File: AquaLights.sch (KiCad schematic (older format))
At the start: 15 parts, among them J2 Raspberry_Pi_2_3, U1 LM2575-5.0BT

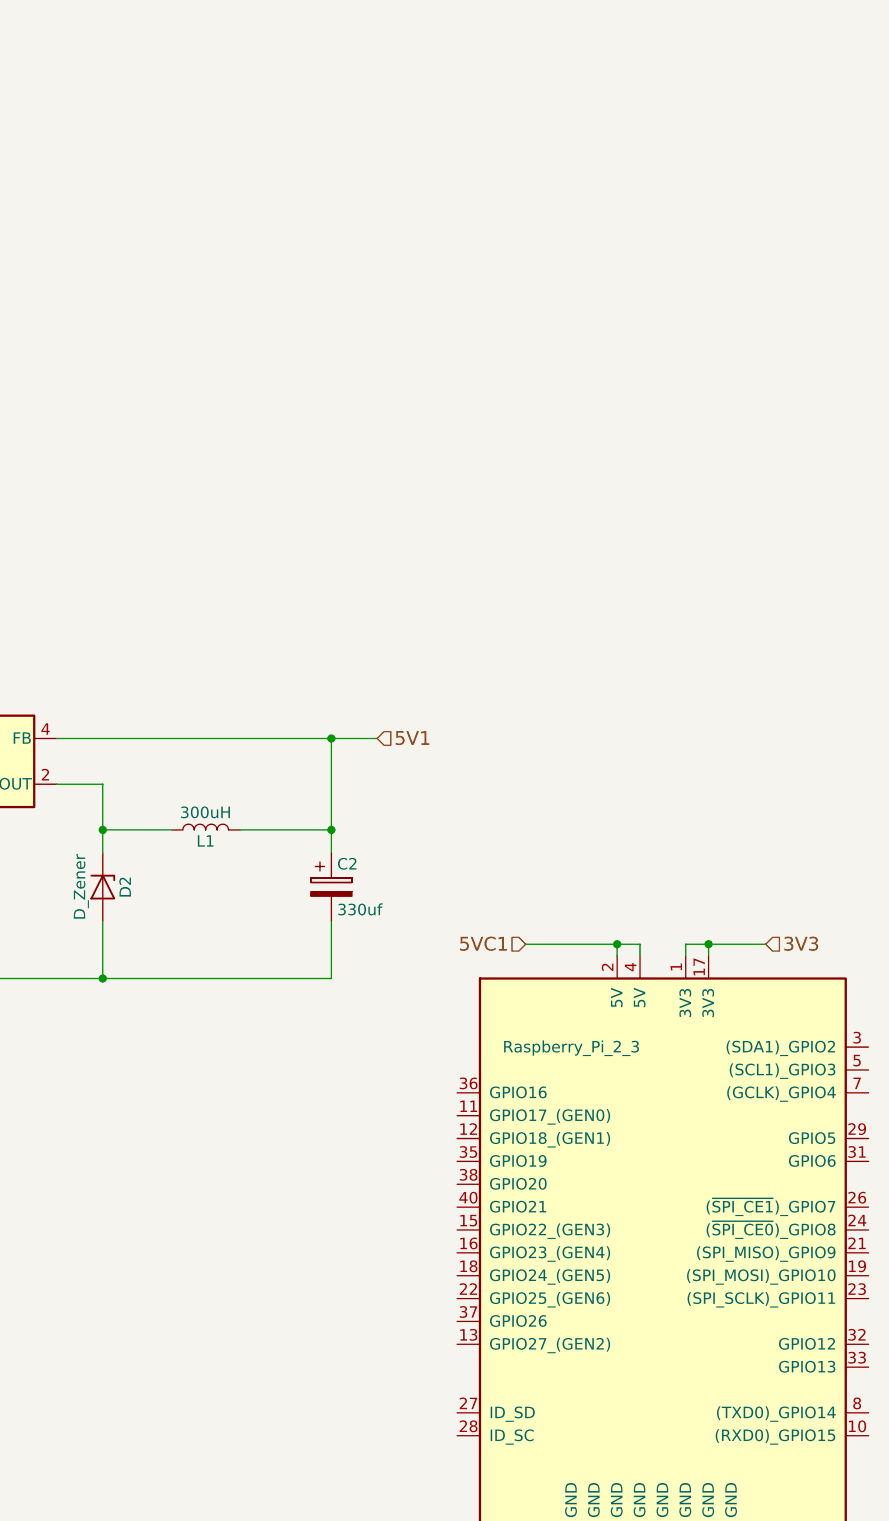
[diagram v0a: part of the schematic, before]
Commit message: Add one PWM Section
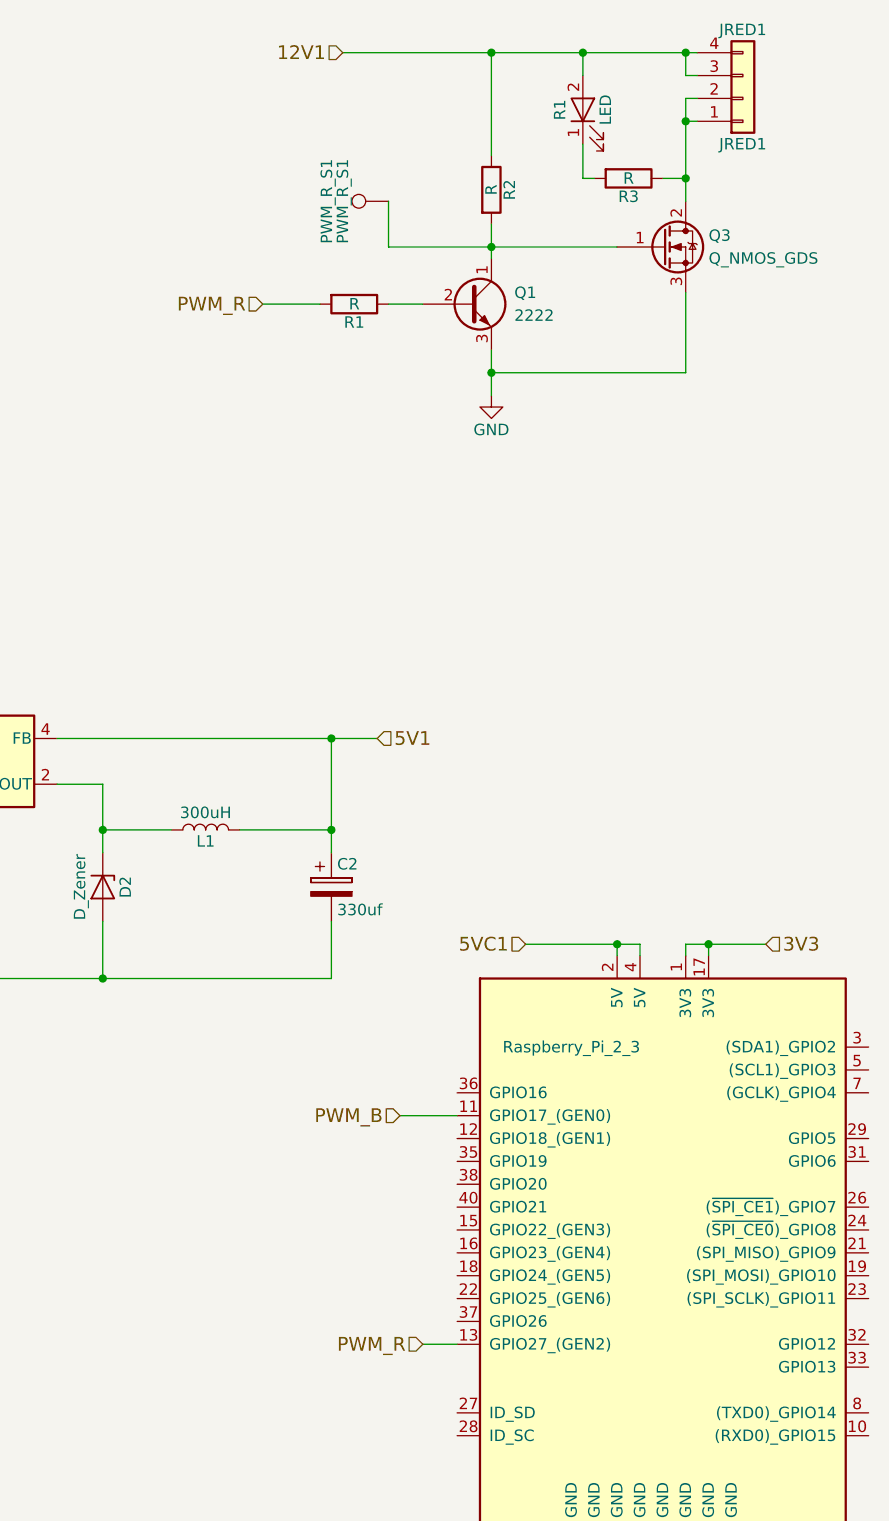
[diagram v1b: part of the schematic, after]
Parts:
- added JRED1: JRED1, symbol Conn_01x04
- added PWM_R_S1: PWM_R_S1, symbol TEST_1P
- added Q1: 2222, symbol Q_NPN_CBE
- added Q3: Q_NMOS_GDS, symbol Q_NMOS_GDS
- added R1, R2, R3: R, symbol R
- added R1: LED, symbol LED
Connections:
- net 12V1: now also JRED1.3 (Pin_3), JRED1.4 (Pin_4), R1.2 (A), R2.1
- net GND: now also Q1.3 (E), Q3.3 (S)
- net PWM_B: now reaches J2.11 (GPIO17_(GEN0))
- net PWM_R: now reaches J2.13 (GPIO27_(GEN2))
- net PWM_R: now also R1.2
- new net: Q1.2 (B), R1.1
- new net: PWM_R_S1.1, Q1.1 (C), Q3.1 (G), R2.2
- new net: JRED1.1 (Pin_1), JRED1.2 (Pin_2), Q3.2 (D), R3.1
- new net: R1.1 (K), R3.2
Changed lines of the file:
@@
 5VC1
 Connection ~ 2200 5600
+Text HLabel 4700 6400 0    60   Input ~ 0
+PWM_R
+Wire Wire Line
+	4700 6400 4850 6400
+Text HLabel 4600 5400 0    60   Input ~ 0
+PWM_B
+Wire Wire Line
+	4600 5400 4850 5400
+Text HLabel 4000 1850 0    60   Input ~ 0
+PWM_R
+$Comp
+L R R1
+U 1 1 5A3322D0
+P 4400 1850
+F 0 "R1" V 4480 1850 50  0000 C CNN
+F 1 "R" V 4400 1850 50  0000 C CNN
+F 2 "" V 4330 1850 50  0001 C CNN
+F 3 "" H 4400 1850 50  0001 C CNN
+	1    4400 1850
+	0    1    1    0
+$EndComp
+Wire Wire Line
+	4000 1850 4250 1850
+$Comp
+L Q_NPN_CBE Q1
+U 1 1 5A3324B5
+P 4900 1850
+F 0 "Q1" H 5100 1900 50  0000 L CNN
+F 1 "2222" H 5100 1800 50  0000 L CNN
+F 2 "" H 5100 1950 50  0001 C CNN
+F 3 "" H 4900 1850 50  0001 C CNN
+	1    4900 1850
+	1    0    0    -1
+$EndComp
+Wire Wire Line
+	4550 1850 4700 1850
+$Comp
+L GND #PWR?
+U 1 1 5A3325C1
+P 5000 2250
+F 0 "#PWR?" H 5000 2000 50  0001 C CNN
+F 1 "GND" H 5000 2100 50  0000 C CNN
+F 2 "" H 5000 2250 50  0001 C CNN
+F 3 "" H 5000 2250 50  0001 C CNN
+	1    5000 2250
+	1    0    0    -1
+$EndComp
+Wire Wire Line
+	5000 2050 5000 2250
+$Comp
+L R R2
+U 1 1 5A33264F
+P 5000 1350
+F 0 "R2" V 5080 1350 50  0000 C CNN
+F 1 "R" V 5000 1350 50  0000 C CNN
+F 2 "" V 4930 1350 50  0001 C CNN
+F 3 "" H 5000 1350 50  0001 C CNN
+	1    5000 1350
+	1    0    0    -1
+$EndComp
+Wire Wire Line
+	5000 1500 5000 1650
+Text HLabel 4350 750  0    60   Input ~ 0
+12V1
+Wire Wire Line
+	5000 750  5000 1200
+$Comp
+L Q_NMOS_GDS Q3
+U 1 1 5A3333B3
+P 5750 1600
+F 0 "Q3" H 5950 1650 50  0000 L CNN
+F 1 "Q_NMOS_GDS" H 5950 1550 50  0000 L CNN
+F 2 "" H 5950 1700 50  0001 C CNN
+F 3 "" H 5750 1600 50  0001 C CNN
+	1    5750 1600
+	1    0    0    -1
+$EndComp
+Wire Wire Line
+	4550 1600 5550 1600
+Connection ~ 5000 1600
+Wire Wire Line
+	5850 1800 5850 2150
+Wire Wire Line
+	5850 2150 5000 2150
+Connection ~ 5000 2150
+$Comp
+L Conn_01x04 JRED1
+U 1 1 5A3334C6
+P 6100 950
+F 0 "JRED1" H 6100 1150 50  0000 C CNN
+F 1 "JRED1" H 6100 650 50  0000 C CNN
+F 2 "" H 6100 950 50  0001 C CNN
+F 3 "" H 6100 950 50  0001 C CNN
+	1    6100 950
+	1    0    0    1
+$EndComp
+Wire Wire Line
+	5850 1400 5850 950
+Wire Wire Line
+	5850 950  5900 950
+Wire Wire Line
+	5900 1050 5850 1050
+Connection ~ 5850 1050
+Wire Wire Line
+	5900 850  5850 850
+Wire Wire Line
+	5850 850  5850 750
+Wire Wire Line
+	4350 750  5900 750
+Connection ~ 5850 750
+Connection ~ 5000 750
+$Comp
+L LED R1
+U 1 1 5A334293
+P 5400 1000
+F 0 "R1" H 5400 1100 50  0000 C CNN
+F 1 "LED" H 5400 900 50  0000 C CNN
+F 2 "" H 5400 1000 50  0001 C CNN
+F 3 "" H 5400 1000 50  0001 C CNN
+	1    5400 1000
+	0    -1   -1   0
+$EndComp
+$Comp
+L R R3
+U 1 1 5A3342DA
+P 5600 1300
+F 0 "R3" V 5680 1300 50  0000 C CNN
+F 1 "R" V 5600 1300 50  0000 C CNN
+F 2 "" V 5530 1300 50  0001 C CNN
+F 3 "" H 5600 1300 50  0001 C CNN
+	1    5600 1300
+	0    1    1    0
+$EndComp
+Wire Wire Line
+	5400 750  5400 850
+Connection ~ 5400 750
+Wire Wire Line
+	5400 1150 5400 1300
+Wire Wire Line
+	5400 1300 5450 1300
+Wire Wire Line
+	5750 1300 5850 1300
+Connection ~ 5850 1300
+$Comp
+L TEST_1P PWM_R_S1
+U 1 1 5A33462D
+P 4550 1400
+F 0 "PWM_R_S1" H 4550 1670 50  0000 C CNN
+F 1 "PWM_R_S1" H 4550 1600 50  0000 C CNN
+F 2 "" H 4750 1400 50  0001 C CNN
+F 3 "" H 4750 1400 50  0001 C CNN
+	1    4550 1400
+	0    -1   -1   0
+$EndComp
+Wire Wire Line
+	4550 1400 4550 1600
 $EndSCHEMATC

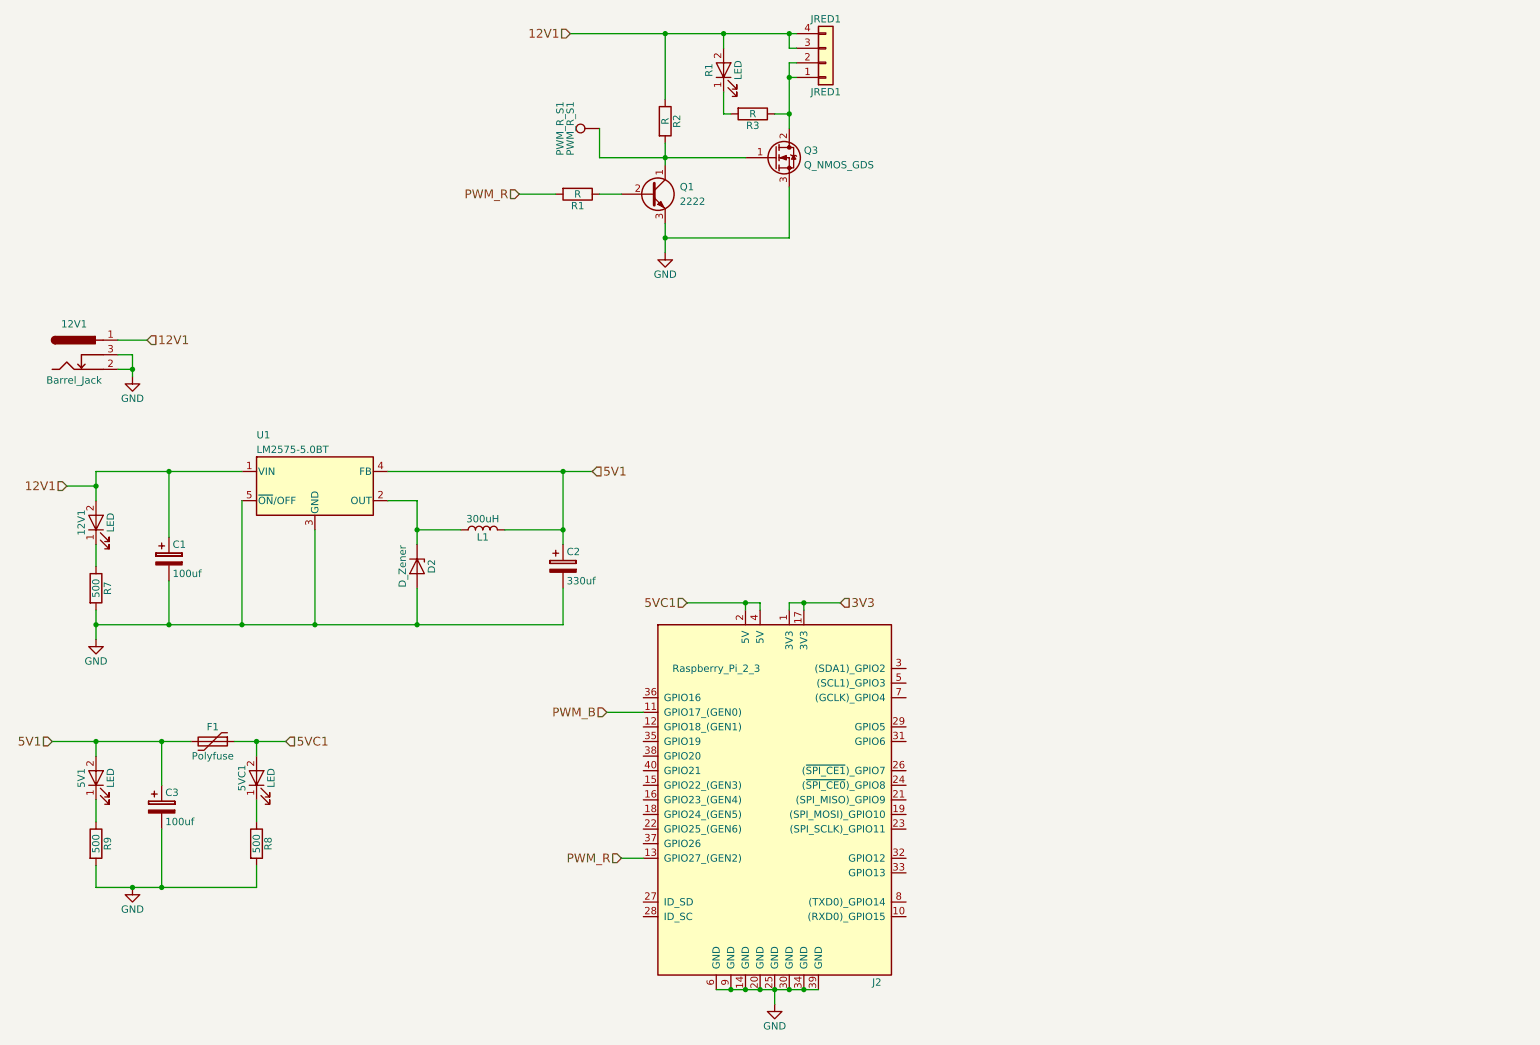
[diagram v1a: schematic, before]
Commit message: Finish PWM Sections
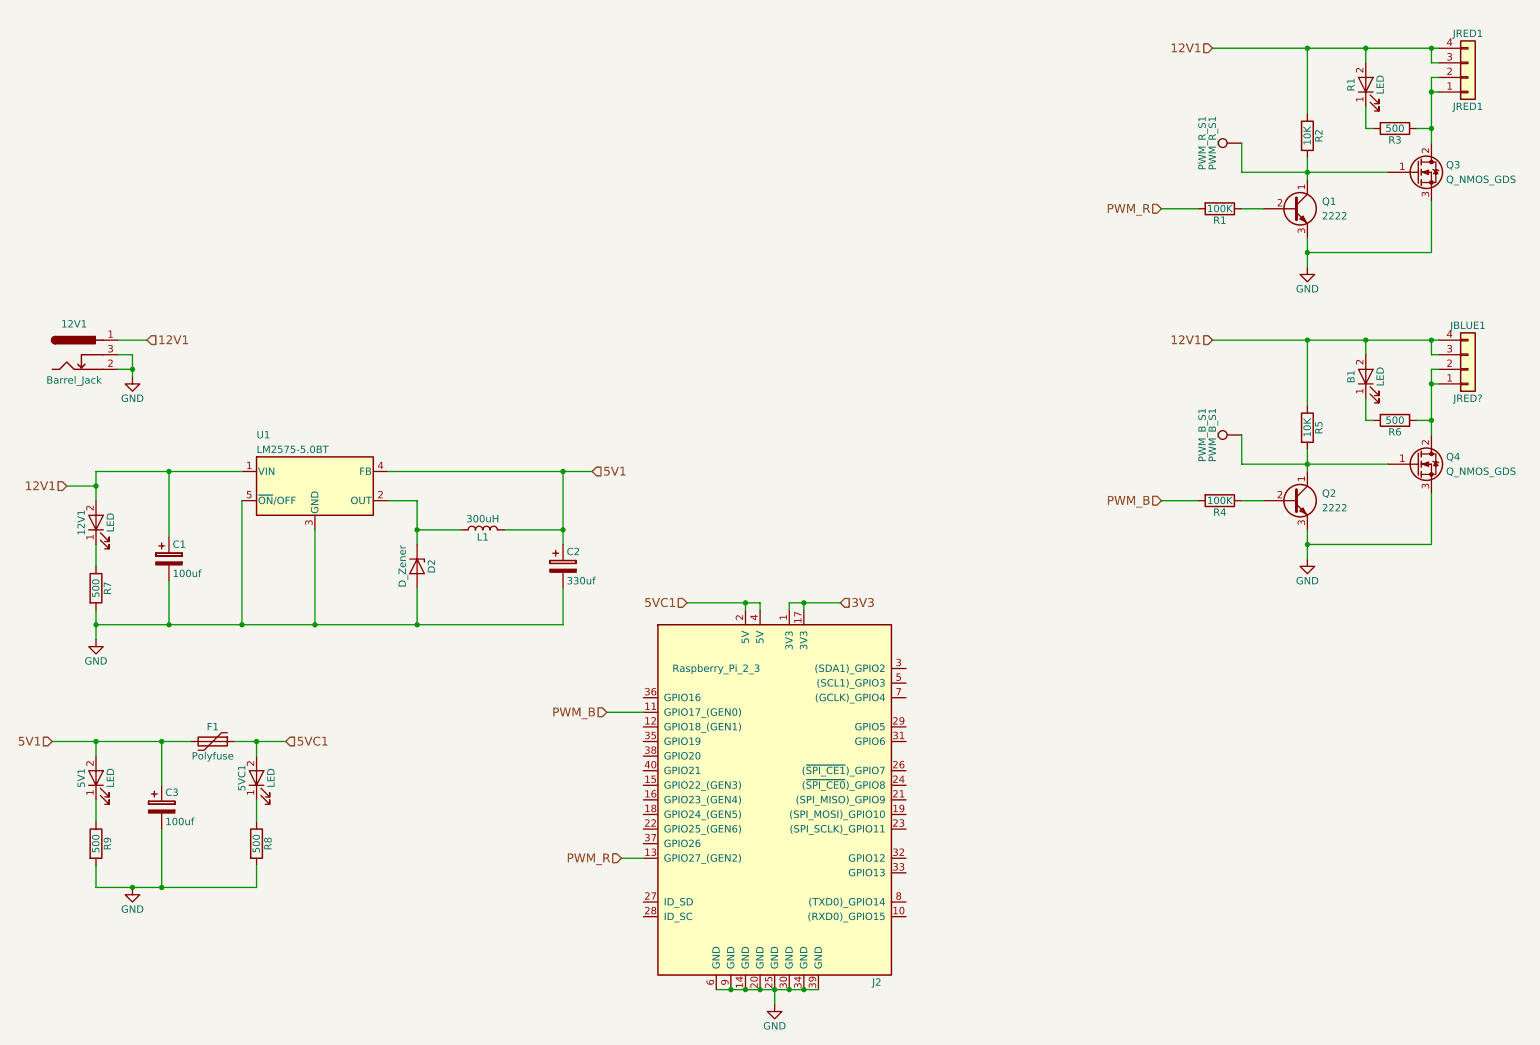
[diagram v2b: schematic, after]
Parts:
- added B1: LED, symbol LED
- added JRED?: JBLUE1, symbol Conn_01x04
- added PWM_B_S1: PWM_B_S1, symbol TEST_1P
- added Q2: 2222, symbol Q_NPN_CBE
- added Q4: Q_NMOS_GDS, symbol Q_NMOS_GDS
- added R4: 100K, symbol R
- added R5: 10K, symbol R
- added R6: 500, symbol R
- R1: value R -> 100K
- R2: value R -> 10K
- R3: value R -> 500
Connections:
- net 12V1: now also B1.2 (A), JRED?.3 (Pin_3), JRED?.4 (Pin_4), R5.1
- net GND: now also Q2.3 (E), Q4.3 (S)
- net PWM_B: now also R4.2
- new net: Q2.2 (B), R4.1
- new net: PWM_B_S1.1, Q2.1 (C), Q4.1 (G), R5.2
- new net: JRED?.1 (Pin_1), JRED?.2 (Pin_2), Q4.2 (D), R6.1
- new net: B1.1 (K), R6.2
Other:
- moved on the sheet: JRED1, PWM_R_S1, Q1, Q3, R1, R2, R3
